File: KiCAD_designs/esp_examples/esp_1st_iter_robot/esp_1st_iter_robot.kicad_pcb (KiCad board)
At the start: 2 copper layers, 22 parts, among them J1 B2B-PH-SM4-TBLFSN, J2 B2B-PH-SM4-TBLFSN, J3 Conn_01x02_Pin, J4 Conn_01x02_Pin, J5 Conn_01x03_Pin, Q1 AO3400A, SW1 KMR223G LFG, SW2 KMR223G LFG, U1 ESP-12F, U2 AMS1117-3.3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

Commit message: esp_bot_fullRoute
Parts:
- moved J3 46.8 mm to (40.3, 32.0), turned to 0 degrees
- moved D2 25.0 mm to (107.6, 32.0), turned to -90 degrees
- moved D1 24.7 mm to (107.9, 67.9), turned to 90 degrees
- moved R2 23.5 mm to (95.7, 36.7)
- moved J4 17.7 mm to (40.3, 39.6)
- moved J5 16.2 mm to (40.3, 56.5), turned to 180 degrees
- moved Q1 16.0 mm to (95.9, 52.8), turned to 90 degrees
- moved R5 13.5 mm to (108.0, 49.4), turned to 90 degrees
- moved SW2 12.7 mm to (95.6, 43.7), turned to -90 degrees
- moved R3 10.7 mm to (92.1, 53.2), turned to 90 degrees
- moved J1 9.74 mm to (90.1, 68.0)
- moved J2 8.96 mm to (45.2, 68.0), turned to 180 degrees
- moved U3 3.09 mm to (51.2, 36.3)
- moved C2 2.36 mm to (65.3, 69.8)
- moved C1 2.36 mm to (61.1, 69.8)
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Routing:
- net Net-(D1-K): track 7.12 -> 81.9 mm
- net VCC: track 101.0 -> 160.2 mm
- net Net-(J3-Pin_1): track 12.6 -> 68.1 mm
- net Net-(J3-Pin_2): track 13.0 -> 65.3 mm
- net Net-(D2-K): track 7.07 -> 44.5 mm
- net Net-(J4-Pin_2): track 38.3 -> 75.4 mm
- net Net-(D1-A): track 7.57 -> 37.1 mm
- net Net-(J1-Pad1): track 9.79 -> 27.3 mm
- net /servo: track 9.89 -> 26.1 mm
- net Net-(U1-GPIO0): track 15.1 -> 26.5 mm
- net Net-(U1-GPIO13): track 28.0 -> 32.2 mm
- net Net-(U1-RST): track 21.4 -> 18.3 mm
- net /DC: track 13.4 -> 15.2 mm
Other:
- board outline added: 85 x 50 mm

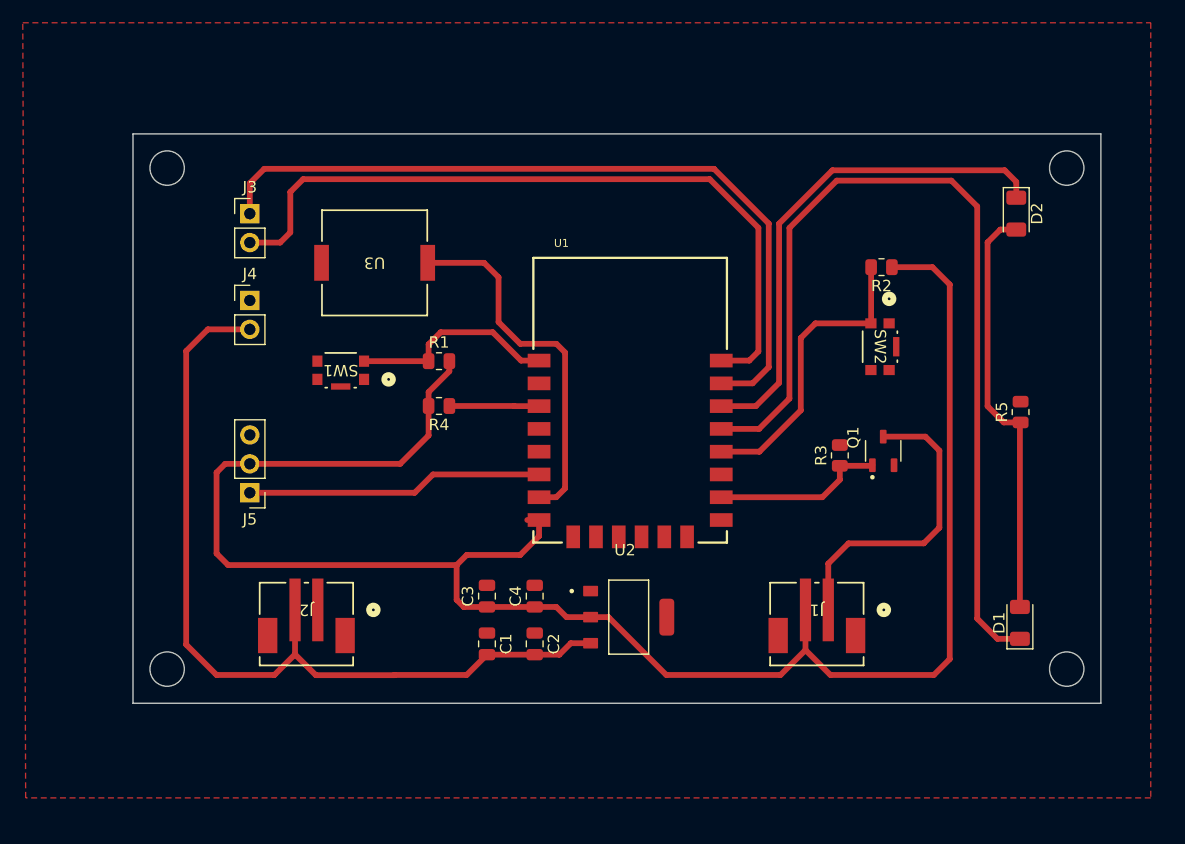
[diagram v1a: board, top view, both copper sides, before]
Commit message: esp_v3_routed with keep-out
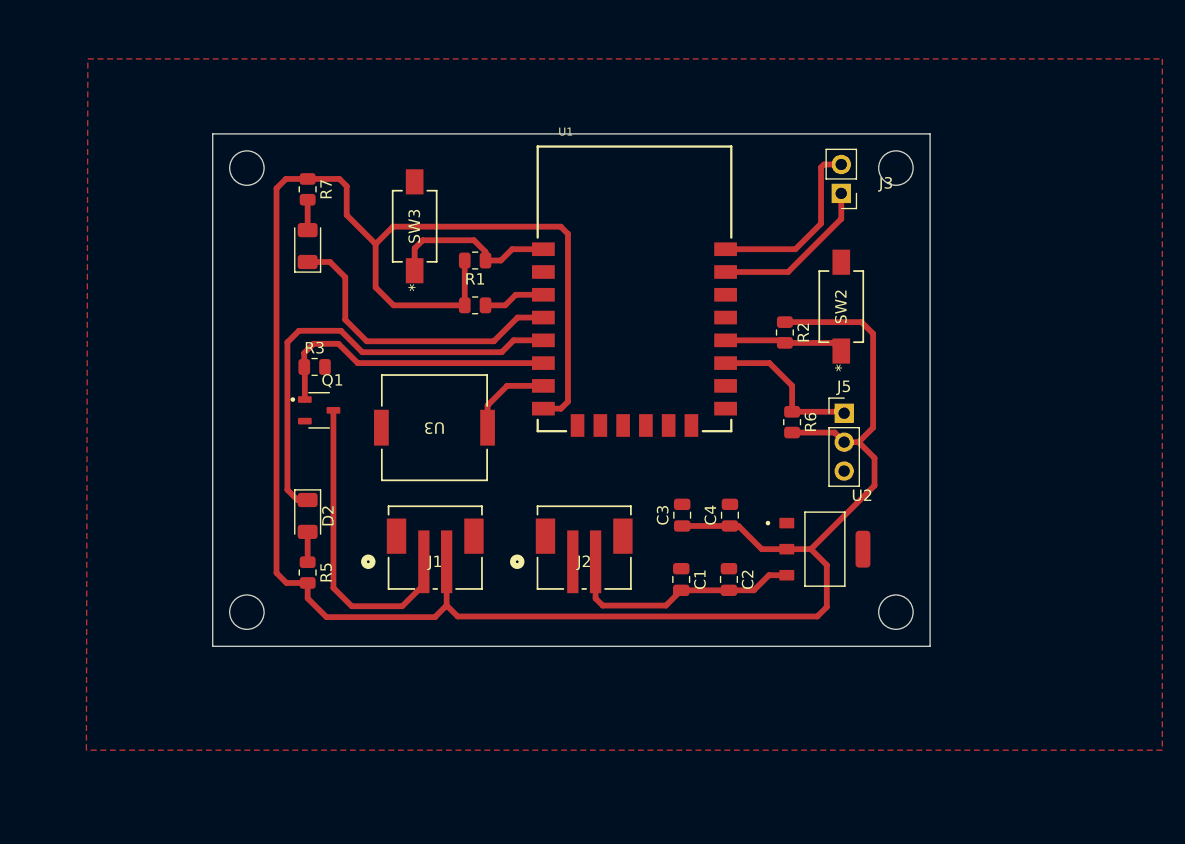
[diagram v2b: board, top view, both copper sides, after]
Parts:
- removed J4: Conn_01x02_Pin, Connector_PinHeader_2.54mm:PinHeader_1x02_P2.54mm_Vertical
- removed SW1: KMR223G LFG, esp_lib:KMR2_G_CNK
- added R6: R, Resistor_SMD:R_0805_2012Metric, F.Cu at (87.9, 50.3)
- added R7: R, Resistor_SMD:R_0805_2012Metric, F.Cu at (45.3, 29.9)
- added SW3: RS-282G05A3-SM RT, esp_lib:RS-282G05A3-SM RT_CNK, F.Cu at (54.7, 33.1)
- SW2: value KMR223G LFG -> RS-282G05A3-SM RT; footprint esp_lib:KMR2_G_CNK -> esp_lib:RS-282G05A3-SM RT_CNK
- moved D1 70.8 mm to (45.3, 34.8)
- moved D2 67.7 mm to (45.3, 58.5)
- moved R5 64.2 mm to (45.3, 63.5), turned to -90 degrees
- moved J5 52.7 mm to (92.5, 49.5), turned to 0 degrees
- moved J3 52.0 mm to (92.2, 30.2), turned to 180 degrees
- moved Q1 49.7 mm to (46.3, 49.3), turned to 0 degrees
- moved R3 46.8 mm to (46.0, 45.5), turned to 0 degrees
- moved J1 34.2 mm to (56.5, 61.3), turned to 0 degrees
- moved J2 25.3 mm to (69.6, 61.3), turned to 0 degrees
- moved C3 18.6 mm to (78.2, 58.5)
- moved C4 18.6 mm to (82.4, 58.5)
- moved U2 18.2 mm to (90.8, 61.5)
- moved C1 18.0 mm to (78.1, 64.1)
- moved C2 18.0 mm to (82.3, 64.1)
- moved U3 15.4 mm to (56.5, 50.8)
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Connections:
- net Net-(U1-GPIO13) renamed /buzzer
- D1 pad 1: Net-(D1-K) -> /LED2
- D2 pad 1: Net-(D2-K) -> /LED1
- D2 pad 2: Net-(D1-A) -> Net-(D2-A)
- R2 pad 2: Net-(U1-GPIO0) -> /boot
- R5 pad 1: Net-(D1-A) -> Net-(D2-A)
- R5 pad 2: GND -> VCC
- SW2 pad 1: unconnected-(SW2-Pad1) -> /boot
- U1 pad 16: /DC -> GND
- U1 pad 17: unconnected-(U1-GPIO2-Pad17) -> /servo
- U1 pad 18: Net-(U1-GPIO0) -> /boot
- U1 pad 19: Net-(D1-K) -> unconnected-(U1-GPIO4-Pad19)
- U1 pad 20: Net-(D2-K) -> unconnected-(U1-GPIO5-Pad20)
- U1 pad 4: unconnected-(U1-GPIO16-Pad4) -> /LED2
- U1 pad 5: unconnected-(U1-GPIO14-Pad5) -> /LED1
- U1 pad 6: /servo -> /DC
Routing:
- net Net-(D1-K): track 81.9 -> 0.00 mm
- net Net-(U2-VIN): track 75.4 -> 21.4 mm
- net Net-(J3-Pin_1): track 68.1 -> 14.3 mm
- net Net-(J3-Pin_2): track 65.3 -> 16.1 mm
- net VCC: track 160.2 -> 208.1 mm
- net Net-(D2-K): track 44.5 -> 0.00 mm
- net /LED1: track 0.00 -> 39.2 mm
- net Net-(D1-A): track 37.1 -> 2.67 mm
- net /LED2: track 0.00 -> 26.6 mm
- net Net-(U1-GPIO0): track 26.5 -> 0.00 mm
- net /buzzer: track 32.2 -> 7.57 mm
- net /servo: track 26.1 -> 13.6 mm
- net /DC: track 15.2 -> 26.1 mm
- net /boot: track 0.00 -> 10.6 mm
- net Net-(U1-RST): track 18.3 -> 15.2 mm
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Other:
- board size 85 x 50 mm -> 63 x 45 mm

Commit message: esp_camRoller
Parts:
- removed R6: R, Resistor_SMD:R_0805_2012Metric
- added J4: B2B-PH-SM4-TBLFSN, esp_lib:CONN_B2B-PH-SM4-TBLFSN_JST, F.Cu at (60.1, 56.7)
- added Q2: AO3400A, esp_lib:SOT95P280X125-3N, F.Cu at (69.3, 59.9)
- added R8: R, Resistor_SMD:R_0805_2012Metric, F.Cu at (69.0, 55.8)
- J5: value Conn_01x03_Pin -> Conn_01x02_Pin; footprint Connector_PinHeader_2.54mm:PinHeader_1x03_P2.54mm_Vertical -> Connector_PinHeader_2.54mm:PinHeader_1x02_P2.54mm_Vertical
- moved R5 31.0 mm to (43.8, 32.6), turned to 90 degrees
- moved D2 21.1 mm to (43.8, 37.5), turned to 90 degrees
- moved C1 18.2 mm to (86.2, 47.9)
- moved C2 18.2 mm to (90.4, 47.9)
- moved U2 17.1 mm to (77.9, 50.3), turned to 180 degrees
- moved C3 13.8 mm to (90.5, 52.2), turned to -90 degrees
- moved J1 9.24 mm to (48.5, 56.7)
- moved J2 9.00 mm to (78.0, 58.0)
- moved J5 8.95 mm to (87.8, 57.1)
- moved U1 7.64 mm to (72.9, 31.1)
- moved C4 7.39 mm to (86.3, 52.2), turned to -90 degrees
- moved R2 6.35 mm to (85.0, 36.5), turned to 90 degrees
- moved U3 4.09 mm to (55.6, 46.8)
- moved SW2 3.40 mm to (89.7, 37.9)
- moved R1 3.28 mm to (56.8, 36.2)
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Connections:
- C1 pad 2: Net-(U2-VIN) -> Net-(J5-Pin_2)
- C2 pad 2: Net-(U2-VIN) -> Net-(J5-Pin_2)
- J2 pad 2: Net-(U2-VIN) -> Net-(J5-Pin_2)
- J5 pad 1: /servo -> GND
- J5 pad 2: VCC -> Net-(J5-Pin_2)
- U1 pad 17: /servo -> /DC2
- U2 pad 3: Net-(U2-VIN) -> Net-(J5-Pin_2)
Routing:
- net /DC2: track 0.00 -> 35.7 mm
- net Net-(J5-Pin_2): track 0.00 -> 32.0 mm
- net Net-(U2-VIN): track 21.4 -> 0.00 mm
- net Net-(J4-Pad1): track 0.00 -> 16.5 mm
- net Net-(J1-Pad1): track 27.0 -> 10.5 mm
- net /servo: track 13.6 -> 0.00 mm
- net /LED1: track 39.2 -> 28.9 mm
- net Net-(J3-Pin_2): track 16.1 -> 8.22 mm
- net Net-(U1-EN): track 5.48 -> 13.2 mm
- net Net-(U1-RST): track 15.2 -> 22.1 mm
- net Net-(J3-Pin_1): track 14.3 -> 8.45 mm
- net /boot: track 10.6 -> 14.0 mm
- net /buzzer: track 7.57 -> 10.9 mm
- net /DC: track 26.1 -> 29.3 mm
- net VCC: track 208.1 -> 210.9 mm
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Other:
- board size 63 x 45 mm -> 57 x 43 mm
